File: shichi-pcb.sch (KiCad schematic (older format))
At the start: 26 parts, among them J1 USB_C_Receptacle_HRO_TYPE-C-3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, J2 Conn_01x04_Male, J3 Conn_01x06_Male, J4 Conn_01x04_Male, J5 Conn_01x01_Male, J6 Conn_01x01_Male, J7 Conn_01x01_Male, SW1 SW_Push, U1 USBLC6-2SC6, U2 ATmega32U4-AU, Y1 Crystal_GND24

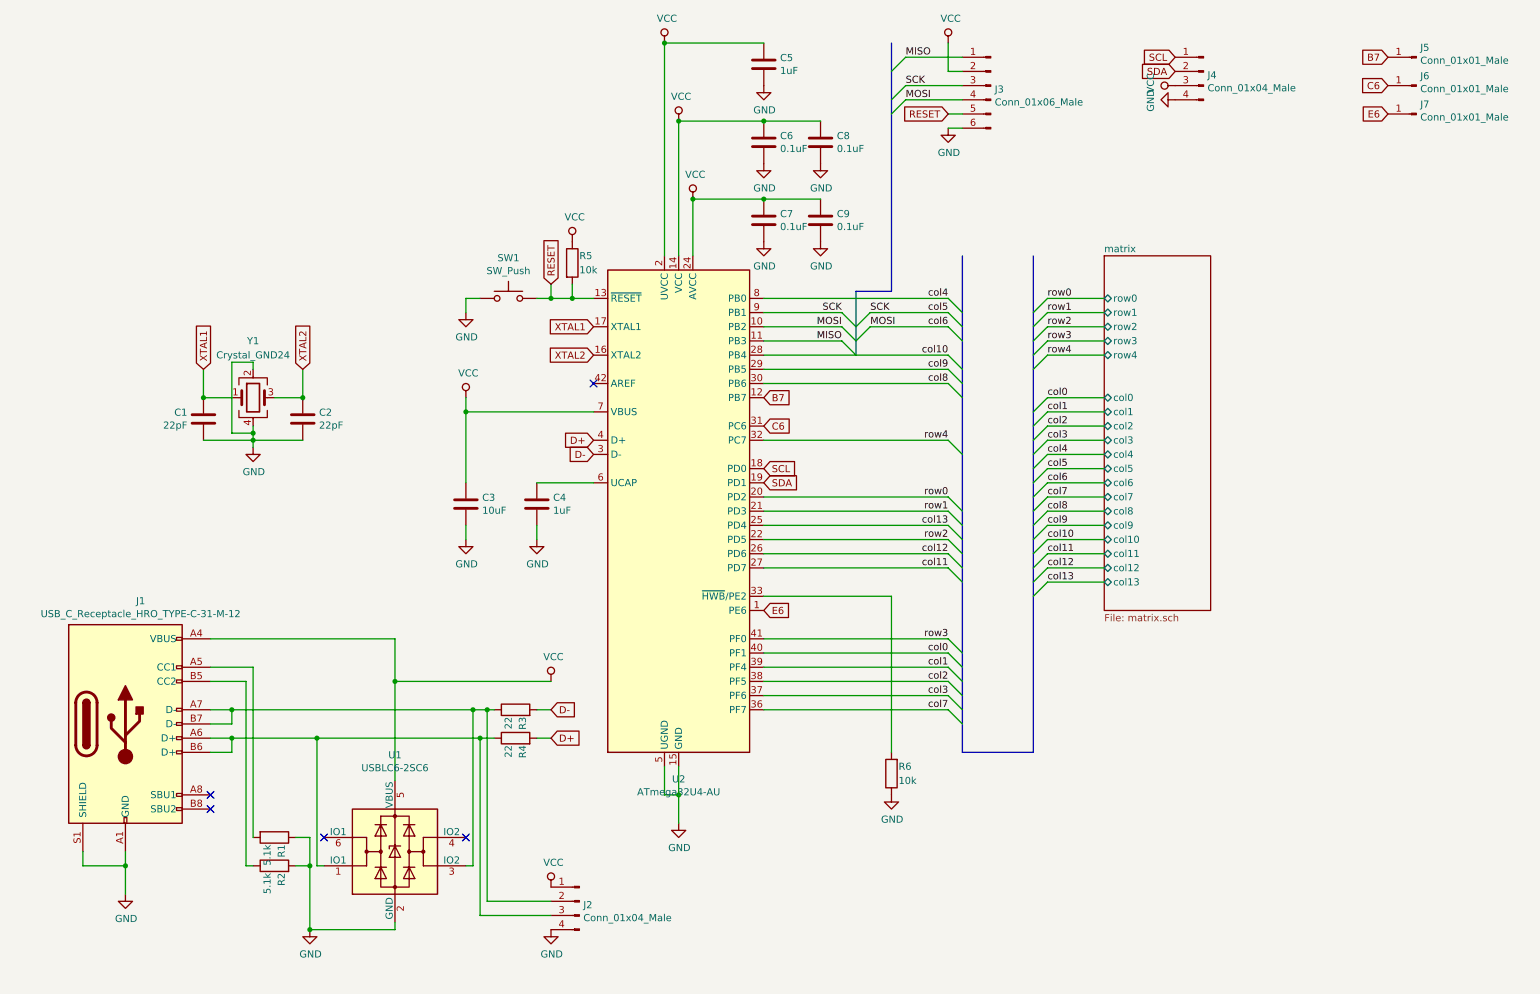
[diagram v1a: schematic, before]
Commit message: Implement over-current protection using polyfuse
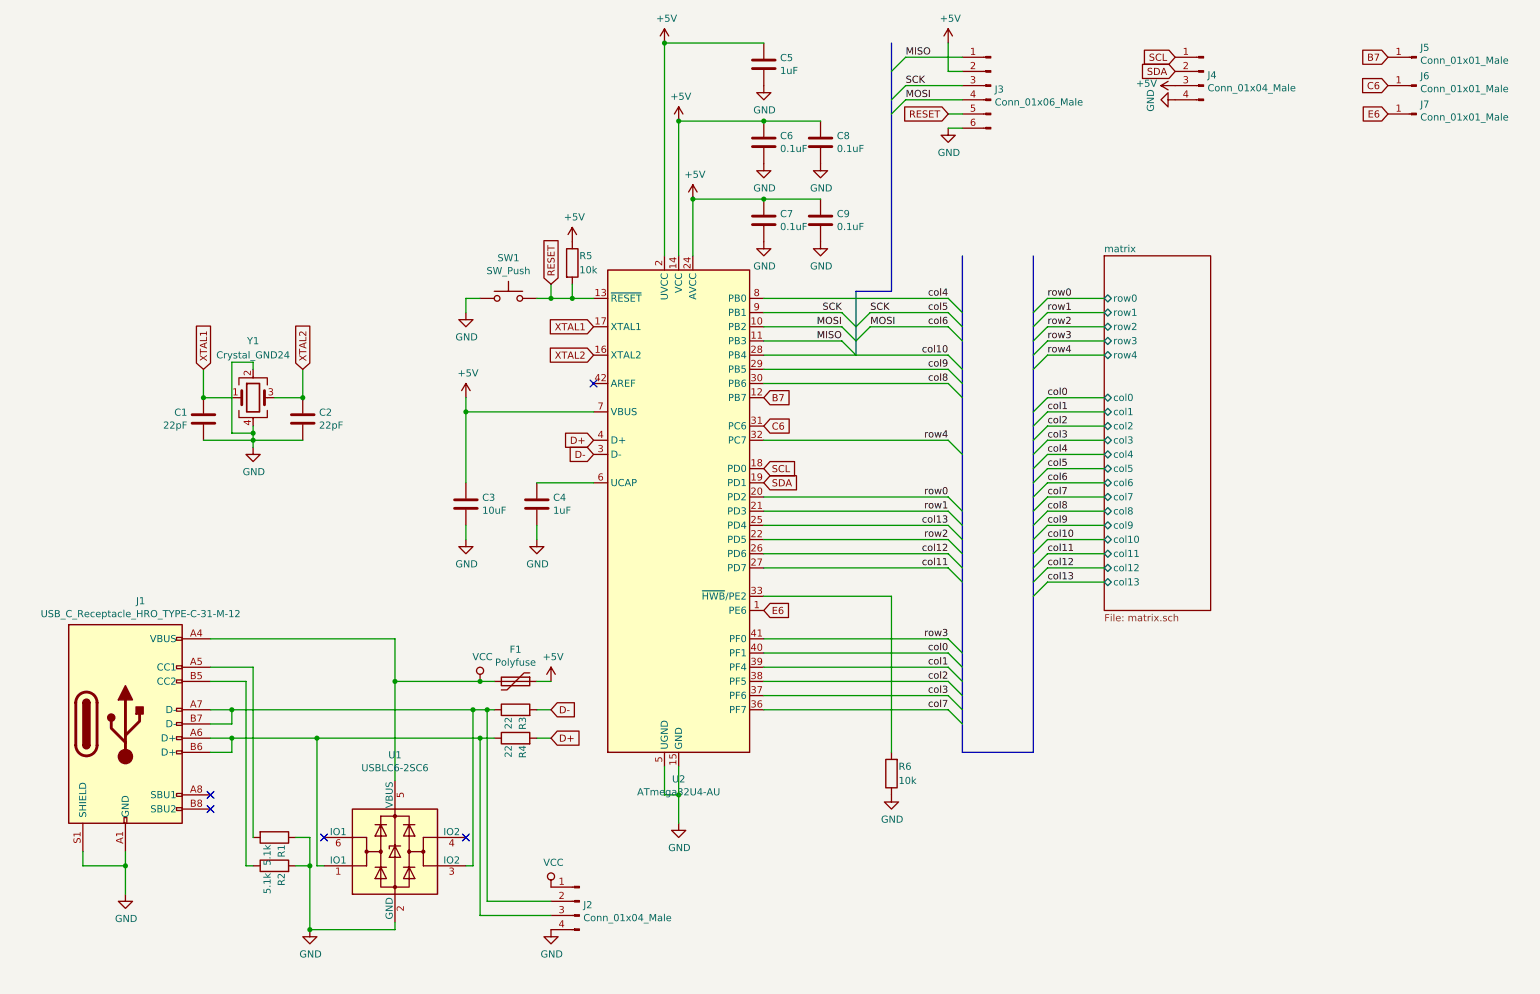
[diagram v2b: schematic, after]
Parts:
- added F1: Polyfuse, Fuse:Fuse_1206_3216Metric_Pad1.42x1.75mm_HandSolder, symbol Device:Polyfuse
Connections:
- net VCC: now also F1.2; no longer C3.1, C5.1, C6.1, C7.1, C8.1, C9.1, J3.2 (Pin_2), J4.3 (Pin_3), R5.1, U2.14 (VCC), U2.2 (UVCC), U2.24 (AVCC), U2.34 (VCC), U2.44 (AVCC), U2.7 (VBUS)
- new net +5V: C3.1, C5.1, C6.1, C7.1, C8.1, C9.1, F1.1, J3.2 (Pin_2), J4.3 (Pin_3), R5.1, U2.14 (VCC), U2.2 (UVCC), U2.24 (AVCC), U2.34 (VCC), U2.44 (AVCC), U2.7 (VBUS)
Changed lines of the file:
@@
 	1850 3750 2000 3750
 $Comp
-L power:VCC #PWR08
+L power:VCC #PWR07
 U 1 1 5CFA87A5
-P 4100 5500
-F 0 "#PWR08" H 4100 5350 50  0001 C CNN
-F 1 "VCC" H 4117 5673 50  0000 C CNN
-F 2 "" H 4100 5500 50  0001 C CNN
-F 3 "" H 4100 5500 50  0001 C CNN
-	1    4100 5500
-	1    0    0    -1
-$EndComp
-$Comp
-L power:VCC #PWR05
-U 1 1 5CFA9EEE
-P 3500 3500
-F 0 "#PWR05" H 3500 3350 50  0001 C CNN
-F 1 "VCC" H 3517 3673 50  0000 C CNN
-F 2 "" H 3500 3500 50  0001 C CNN
-F 3 "" H 3500 3500 50  0001 C CNN
-	1    3500 3500
-	1    0    0    -1
-$EndComp
-$Comp
-L power:VCC #PWR011
-U 1 1 5CFABEFF
-P 4250 2400
-F 0 "#PWR011" H 4250 2250 50  0001 C CNN
-F 1 "VCC" H 4267 2573 50  0000 C CNN
-F 2 "" H 4250 2400 50  0001 C CNN
-F 3 "" H 4250 2400 50  0001 C CNN
-	1    4250 2400
-	1    0    0    -1
-$EndComp
-$Comp
-L power:VCC #PWR012
-U 1 1 5CFACAC0
-P 4900 1000
-F 0 "#PWR012" H 4900 850 50  0001 C CNN
-F 1 "VCC" H 4917 1173 50  0000 C CNN
-F 2 "" H 4900 1000 50  0001 C CNN
-F 3 "" H 4900 1000 50  0001 C CNN
-	1    4900 1000
-	1    0    0    -1
-$EndComp
-Connection ~ 4900 1000
-$Comp
-L power:VCC #PWR013
-U 1 1 5CFADCFF
-P 5000 1550
-F 0 "#PWR013" H 5000 1400 50  0001 C CNN
-F 1 "VCC" H 5017 1723 50  0000 C CNN
-F 2 "" H 5000 1550 50  0001 C CNN
-F 3 "" H 5000 1550 50  0001 C CNN
-	1    5000 1550
-	1    0    0    -1
-$EndComp
-Connection ~ 5000 1550
-$Comp
-L power:VCC #PWR015
-U 1 1 5CFAE409
-P 5100 2100
-F 0 "#PWR015" H 5100 1950 50  0001 C CNN
-F 1 "VCC" H 5117 2273 50  0000 C CNN
-F 2 "" H 5100 2100 50  0001 C CNN
-F 3 "" H 5100 2100 50  0001 C CNN
-	1    5100 2100
-	1    0    0    -1
-$EndComp
-Connection ~ 5100 2100
-$Comp
-L power:VCC #PWR022
-U 1 1 5CFAE805
-P 6900 1000
-F 0 "#PWR022" H 6900 850 50  0001 C CNN
-F 1 "VCC" H 6917 1173 50  0000 C CNN
-F 2 "" H 6900 1000 50  0001 C CNN
-F 3 "" H 6900 1000 50  0001 C CNN
-	1    6900 1000
+P 3600 5500
+F 0 "#PWR07" H 3600 5350 50  0001 C CNN
+F 1 "VCC" H 3617 5673 50  0000 C CNN
+F 2 "" H 3600 5500 50  0001 C CNN
+F 3 "" H 3600 5500 50  0001 C CNN
+	1    3600 5500
 	1    0    0    -1
 $EndComp
@@
 $EndComp
 $Comp
-L power:GND #PWR021
+L power:GND #PWR022
 U 1 1 5CFB1587
 P 6500 6300
-F 0 "#PWR021" H 6500 6050 50  0001 C CNN
+F 0 "#PWR022" H 6500 6050 50  0001 C CNN
 F 1 "GND" H 6505 6127 50  0000 C CNN
 F 2 "" H 6500 6300 50  0001 C CNN
@@
 $EndComp
 $Comp
-L power:GND #PWR014
+L power:GND #PWR015
 U 1 1 5CFB1FF4
 P 5000 6500
-F 0 "#PWR014" H 5000 6250 50  0001 C CNN
+F 0 "#PWR015" H 5000 6250 50  0001 C CNN
 F 1 "GND" H 5005 6327 50  0000 C CNN
 F 2 "" H 5000 6500 50  0001 C CNN
@@
 $EndComp
 $Comp
-L power:GND #PWR07
+L power:GND #PWR08
 U 1 1 5CFB2640
 P 4000 4500
-F 0 "#PWR07" H 4000 4250 50  0001 C CNN
+F 0 "#PWR08" H 4000 4250 50  0001 C CNN
 F 1 "GND" H 4005 4327 50  0000 C CNN
 F 2 "" H 4000 4500 50  0001 C CNN
@@
 $EndComp
 $Comp
-L power:GND #PWR018
+L power:GND #PWR019
 U 1 1 5CFB4E50
 P 5600 2400
-F 0 "#PWR018" H 5600 2150 50  0001 C CNN
+F 0 "#PWR019" H 5600 2150 50  0001 C CNN
 F 1 "GND" H 5605 2227 50  0000 C CNN
 F 2 "" H 5600 2400 50  0001 C CNN
@@
 $EndComp
 $Comp
-L power:GND #PWR020
+L power:GND #PWR021
 U 1 1 5CFB56F6
 P 6000 2400
-F 0 "#PWR020" H 6000 2150 50  0001 C CNN
+F 0 "#PWR021" H 6000 2150 50  0001 C CNN
 F 1 "GND" H 6005 2227 50  0000 C CNN
 F 2 "" H 6000 2400 50  0001 C CNN
@@
 $EndComp
 $Comp
-L power:GND #PWR017
+L power:GND #PWR018
 U 1 1 5CFB5A7D
 P 5600 1850
-F 0 "#PWR017" H 5600 1600 50  0001 C CNN
+F 0 "#PWR018" H 5600 1600 50  0001 C CNN
 F 1 "GND" H 5605 1677 50  0000 C CNN
 F 2 "" H 5600 1850 50  0001 C CNN
@@
 $EndComp
 $Comp
-L power:GND #PWR019
+L power:GND #PWR020
 U 1 1 5CFB605F
 P 6000 1850
-F 0 "#PWR019" H 6000 1600 50  0001 C CNN
+F 0 "#PWR020" H 6000 1600 50  0001 C CNN
 F 1 "GND" H 6005 1677 50  0000 C CNN
 F 2 "" H 6000 1850 50  0001 C CNN
@@
 $EndComp
 $Comp
-L power:GND #PWR016
+L power:GND #PWR017
 U 1 1 5CFB6455
 P 5600 1300
-F 0 "#PWR016" H 5600 1050 50  0001 C CNN
+F 0 "#PWR017" H 5600 1050 50  0001 C CNN
 F 1 "GND" H 5605 1127 50  0000 C CNN
 F 2 "" H 5600 1300 50  0001 C CNN
@@
 $EndComp
 $Comp
-L power:GND #PWR023
+L power:GND #PWR024
 U 1 1 5CFB6809
 P 6900 1600
-F 0 "#PWR023" H 6900 1350 50  0001 C CNN
+F 0 "#PWR024" H 6900 1350 50  0001 C CNN
 F 1 "GND" H 6905 1427 50  0000 C CNN
 F 2 "" H 6900 1600 50  0001 C CNN
@@
 	4000 5700 4100 5700
 Wire Wire Line
-	3000 5500 4100 5500
-$Comp
-L power:VCC #PWR09
-U 1 1 5D04B89F
-P 4100 6950
-F 0 "#PWR09" H 4100 6800 50  0001 C CNN
-F 1 "VCC" H 4117 7123 50  0000 C CNN
-F 2 "" H 4100 6950 50  0001 C CNN
-F 3 "" H 4100 6950 50  0001 C CNN
-	1    4100 6950
-	1    0    0    -1
-$EndComp
-$Comp
-L power:GND #PWR010
+	3000 5500 3600 5500
+$Comp
+L power:GND #PWR011
 U 1 1 5CFB0CA6
 P 4100 7250
-F 0 "#PWR010" H 4100 7000 50  0001 C CNN
+F 0 "#PWR011" H 4100 7000 50  0001 C CNN
 F 1 "GND" H 4105 7077 50  0000 C CNN
 F 2 "" H 4100 7250 50  0001 C CNN
@@
 $EndComp
 $Comp
-L power:VCC #PWR024
-U 1 1 5D01C4D7
-P 8500 1300
-F 0 "#PWR024" H 8500 1150 50  0001 C CNN
-F 1 "VCC" H 8517 1473 50  0000 C CNN
-F 2 "" H 8500 1300 50  0001 C CNN
-F 3 "" H 8500 1300 50  0001 C CNN
-	1    8500 1300
-	0    -1   -1   0
-$EndComp
-$Comp
-L power:GND #PWR025
+L power:GND #PWR026
 U 1 1 5D01D767
 P 8500 1400
-F 0 "#PWR025" H 8500 1150 50  0001 C CNN
+F 0 "#PWR026" H 8500 1150 50  0001 C CNN
 F 1 "GND" H 8505 1227 50  0000 C CNN
 F 2 "" H 8500 1400 50  0001 C CNN
@@
 	-1   0    0    -1
 $EndComp
+$Comp
+L Device:Polyfuse F1
+U 1 1 5D00DD08
+P 3850 5500
+F 0 "F1" V 3625 5500 50  0000 C CNN
+F 1 "Polyfuse" V 3716 5500 50  0000 C CNN
+F 2 "Fuse:Fuse_1206_3216Metric_Pad1.42x1.75mm_HandSolder" H 3900 5300 50  0001 L CNN
+F 3 "~" H 3850 5500 50  0001 C CNN
+	1    3850 5500
+	0    1    1    0
+$EndComp
+Wire Wire Line
+	3700 5500 3600 5500
+Connection ~ 3600 5500
+$Comp
+L power:+5V #PWR09
+U 1 1 5D0148B8
+P 4100 5500
+F 0 "#PWR09" H 4100 5350 50  0001 C CNN
+F 1 "+5V" H 4115 5673 50  0000 C CNN
+F 2 "" H 4100 5500 50  0001 C CNN
+F 3 "" H 4100 5500 50  0001 C CNN
+	1    4100 5500
+	1    0    0    -1
+$EndComp
+Wire Wire Line
+	4000 5500 4100 5500
+$Comp
+L power:+5V #PWR05
+U 1 1 5D02176A
+P 3500 3500
+F 0 "#PWR05" H 3500 3350 50  0001 C CNN
+F 1 "+5V" H 3515 3673 50  0000 C CNN
+F 2 "" H 3500 3500 50  0001 C CNN
+F 3 "" H 3500 3500 50  0001 C CNN
+	1    3500 3500
+	1    0    0    -1
+$EndComp
+$Comp
+L power:+5V #PWR012
+U 1 1 5D02341D
+P 4250 2400
+F 0 "#PWR012" H 4250 2250 50  0001 C CNN
+F 1 "+5V" H 4265 2573 50  0000 C CNN
+F 2 "" H 4250 2400 50  0001 C CNN
+F 3 "" H 4250 2400 50  0001 C CNN
+	1    4250 2400
+	1    0    0    -1
+$EndComp
+$Comp
+L power:+5V #PWR016
+U 1 1 5D026371
+P 5100 2100
+F 0 "#PWR016" H 5100 1950 50  0001 C CNN
+F 1 "+5V" H 5115 2273 50  0000 C CNN
+F 2 "" H 5100 2100 50  0001 C CNN
+F 3 "" H 5100 2100 50  0001 C CNN
+	1    5100 2100
+	1    0    0    -1
+$EndComp
+Connection ~ 5100 2100
+$Comp
+L power:+5V #PWR014
+U 1 1 5D02731A
+P 5000 1550
+F 0 "#PWR014" H 5000 1400 50  0001 C CNN
+F 1 "+5V" H 5015 1723 50  0000 C CNN
+F 2 "" H 5000 1550 50  0001 C CNN
+F 3 "" H 5000 1550 50  0001 C CNN
+	1    5000 1550
+	1    0    0    -1
+$EndComp
+Connection ~ 5000 1550
+$Comp
+L power:+5V #PWR013
+U 1 1 5D02771F
+P 4900 1000
+F 0 "#PWR013" H 4900 850 50  0001 C CNN
+F 1 "+5V" H 4915 1173 50  0000 C CNN
+F 2 "" H 4900 1000 50  0001 C CNN
+F 3 "" H 4900 1000 50  0001 C CNN
+	1    4900 1000
+	1    0    0    -1
+$EndComp
+Connection ~ 4900 1000
+$Comp
+L power:+5V #PWR023
+U 1 1 5D027C55
+P 6900 1000
+F 0 "#PWR023" H 6900 850 50  0001 C CNN
+F 1 "+5V" H 6915 1173 50  0000 C CNN
+F 2 "" H 6900 1000 50  0001 C CNN
+F 3 "" H 6900 1000 50  0001 C CNN
+	1    6900 1000
+	1    0    0    -1
+$EndComp
+$Comp
+L power:+5V #PWR025
+U 1 1 5D0288AC
+P 8500 1300
+F 0 "#PWR025" H 8500 1150 50  0001 C CNN
+F 1 "+5V" V 8515 1428 50  0000 L CNN
+F 2 "" H 8500 1300 50  0001 C CNN
+F 3 "" H 8500 1300 50  0001 C CNN
+	1    8500 1300
+	0    -1   -1   0
+$EndComp
 Wire Wire Line
 	5600 3200 6900 3200
@@
 Wire Bus Line
 	7500 2500 7500 6000
+$Comp
+L power:VCC #PWR010
+U 1 1 5D05176C
+P 4100 6950
+F 0 "#PWR010" H 4100 6800 50  0001 C CNN
+F 1 "VCC" H 4117 7123 50  0000 C CNN
+F 2 "" H 4100 6950 50  0001 C CNN
+F 3 "" H 4100 6950 50  0001 C CNN
+	1    4100 6950
+	1    0    0    -1
+$EndComp
 $EndSCHEMATC

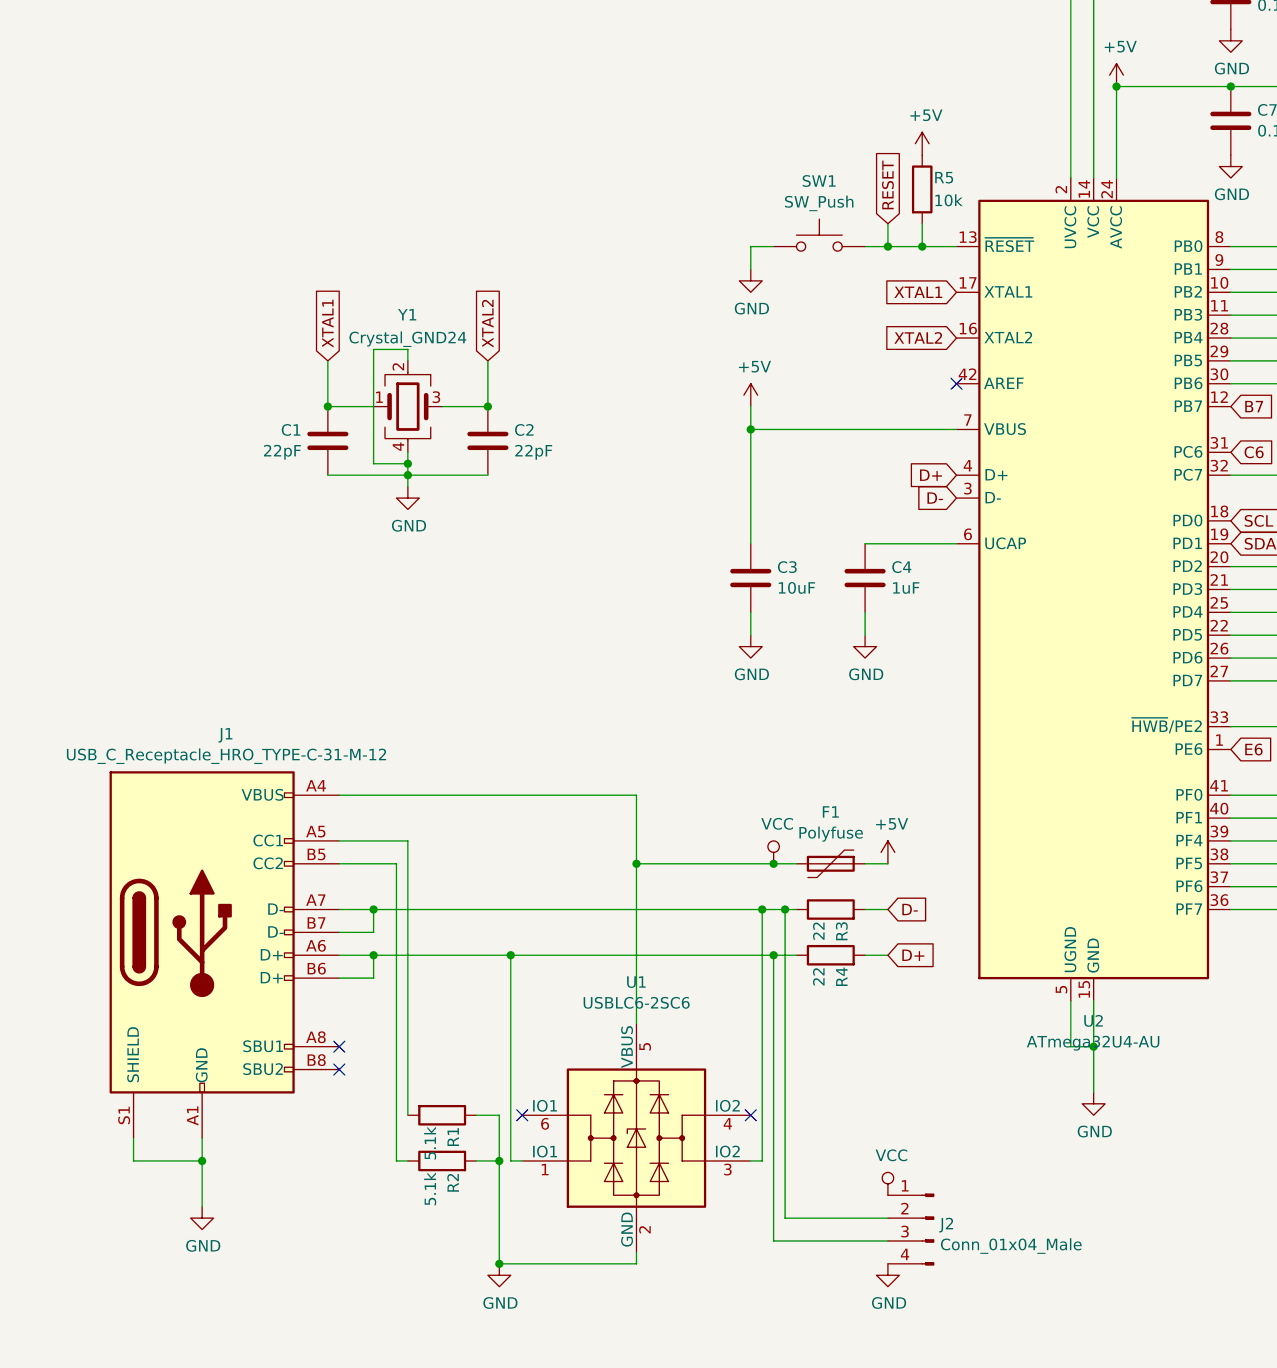
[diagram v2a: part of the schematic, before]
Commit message: Make ESD protection component mandatory in schematic
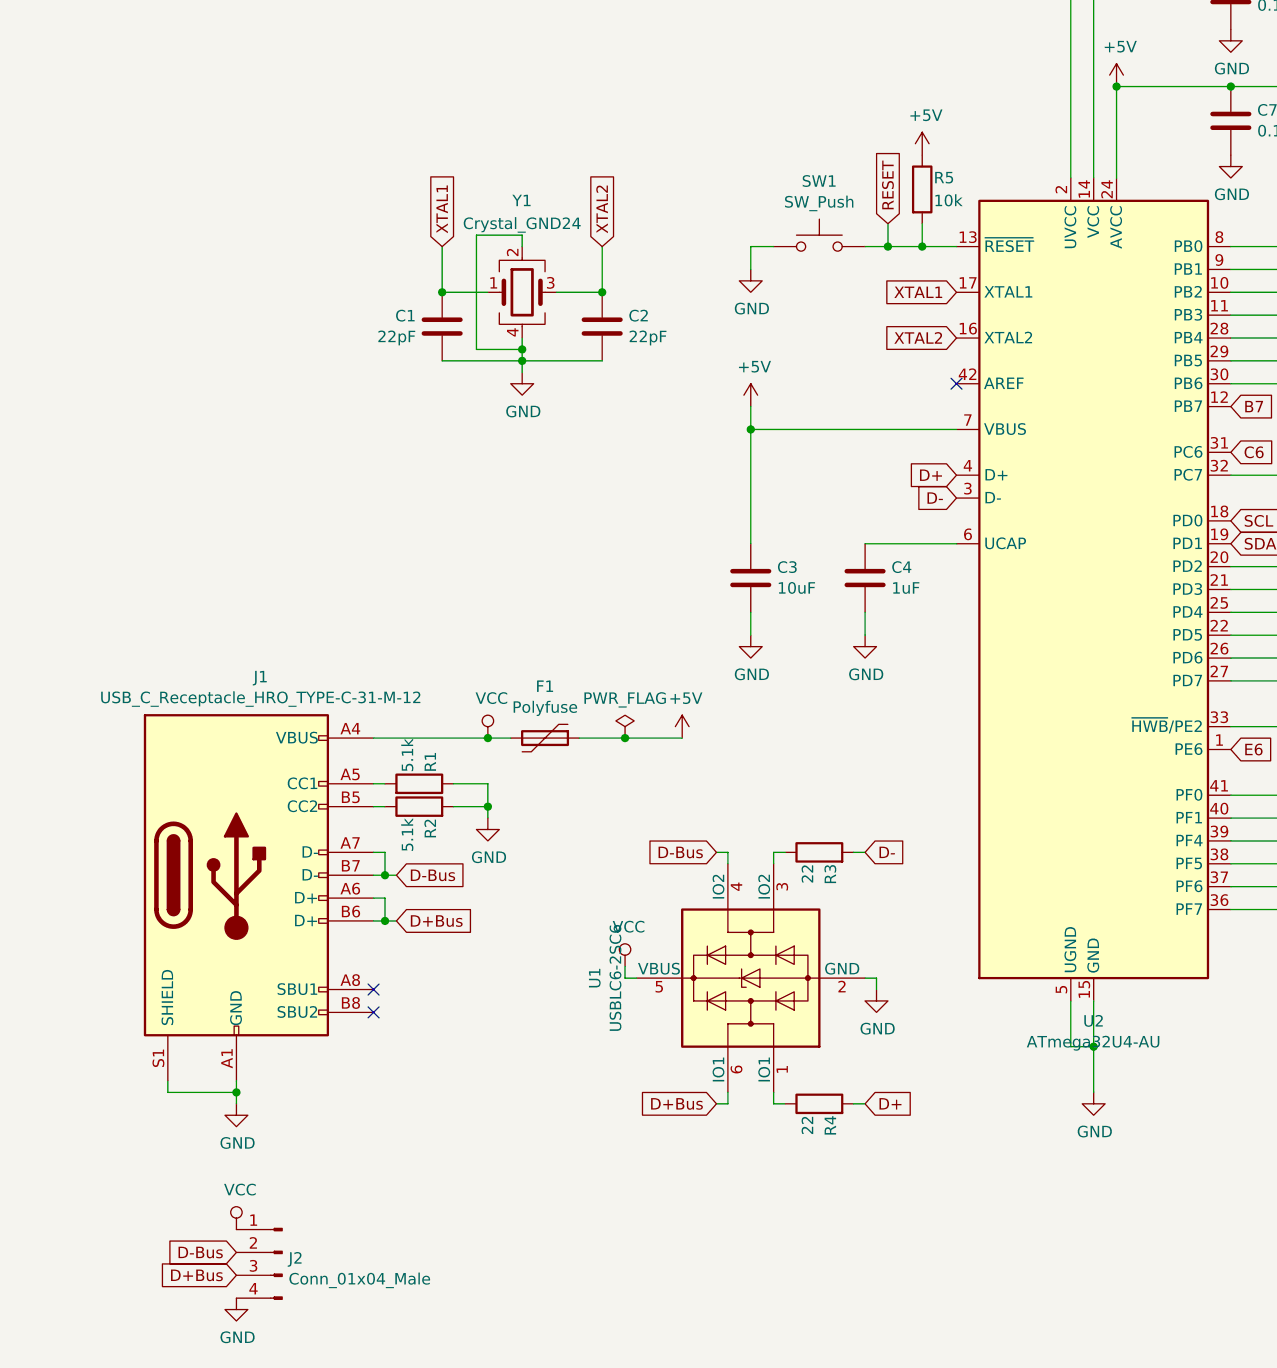
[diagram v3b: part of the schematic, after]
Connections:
- net D+Bus: now reaches J1.A6 (D+), J1.B6 (D+), J2.3 (Pin_3)
- net D+Bus: now also U1.6 (IO1); no longer R4.1, U1.1 (IO1)
- net D-Bus: now reaches J1.A7 (D-), J1.B7 (D-), J2.2 (Pin_2)
- net D-Bus: now also U1.4 (IO2); no longer R3.1, U1.3 (IO2)
- new net: R4.1, U1.1 (IO1)
- new net: R3.1, U1.3 (IO2)
- no-connect marks 5 -> 3
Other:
- moved on the sheet: C1, C2, F1, J1, J2, R1, R2, R3, R4, U1, Y1
